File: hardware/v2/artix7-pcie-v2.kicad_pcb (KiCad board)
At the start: 4 copper layers, 60 x 51 mm, 183 parts, among them J1 Conn_02x20_Odd_Even, J10 USB_B_Micro, J2 Conn_02x20_Odd_Even, J3 JTAG_EN, J4 USB3_A, J5 USB3_A_AS_PCIE, J6 JTAG, J7 Conn_01x02, J8 SER, SW1 PROG, SW2 SW_SPST, U1 XC7A75T-FGG484, U2 W25Q64JVSSIM, U3 LP5907MFX, U4 5P49V6965A000NLGI, U5 TPS82130SILT, U6 TPS82150SILT, U7 TPS82150SILT, U8 TPS82130SILT, U9 TPS82150SILT, X1 25MHz/10pF

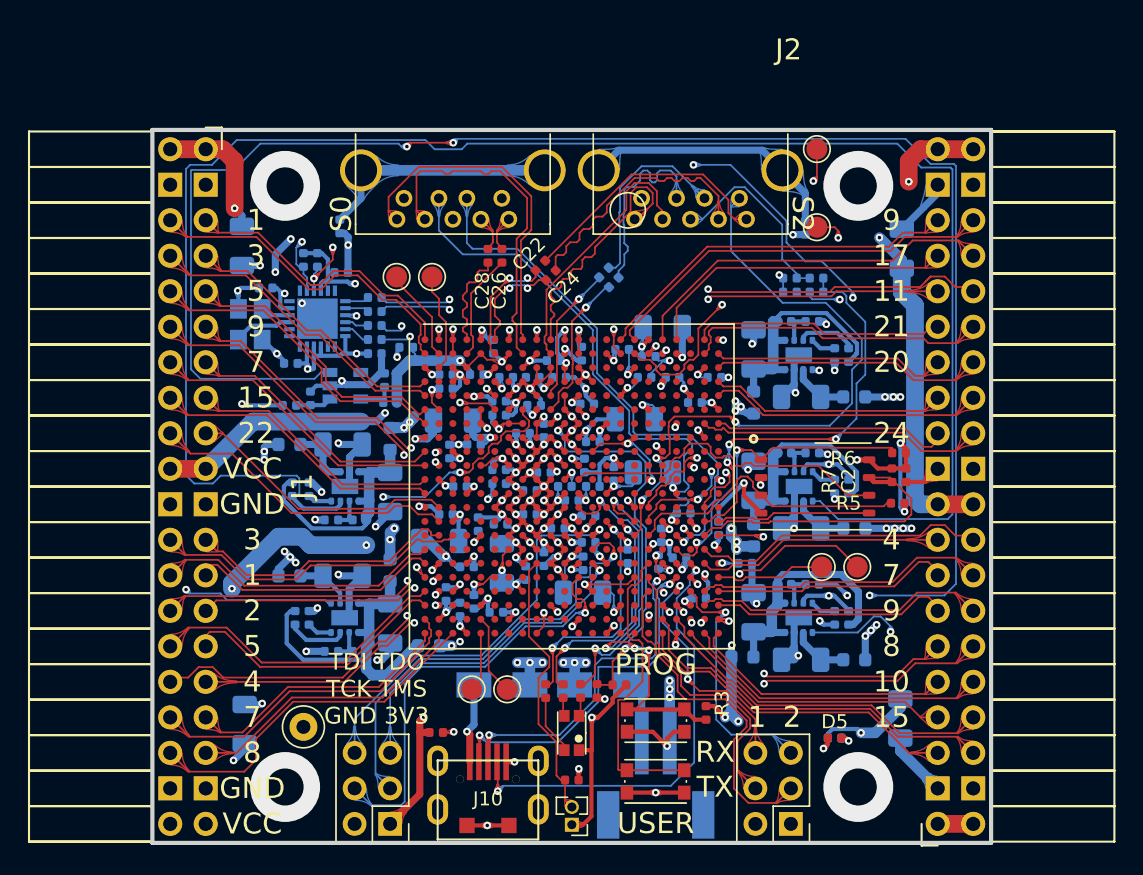
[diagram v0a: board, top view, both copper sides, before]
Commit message: v2 progress commit : serdes lanes all deskewed
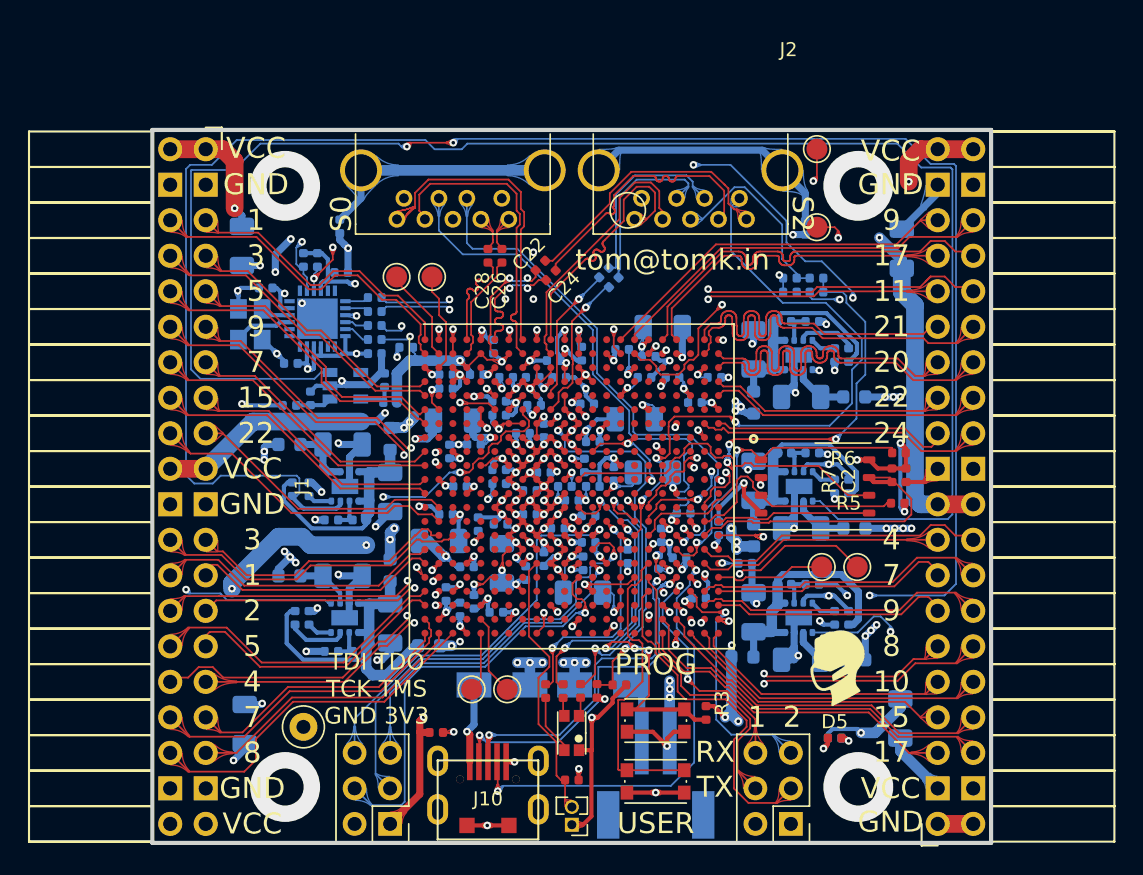
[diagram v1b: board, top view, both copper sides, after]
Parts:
- added G***: LOGO, artix7-pcie-v2:mask, F.Cu at (160.1, 99.8)
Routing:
- net /artix7-pcie-v2-bank14/IO_L20_16_P: track 19.4 -> 29.0 mm
- net /artix7-pcie-v2-bank14/IO_L20_16_N: track 16.7 -> 26.3 mm
- net /artix7-pcie-v2-bank14/IO_L21_16_P: track 21.8 -> 28.9 mm
- net /artix7-pcie-v2-bank14/IO_L21_16_N: track 18.1 -> 25.2 mm
- net /artix7-pcie-v2-serdes/S0_RX_N: track 24.5 -> 21.8 mm
- net /artix7-pcie-v2-serdes/S0_RX_P: track 24.4 -> 21.8 mm
- net /artix7-pcie-v2-bank14/IO_L17_16_N: track 22.5 -> 25.1 mm
- net /artix7-pcie-v2-bank14/IO_L17_16_P: track 26.6 -> 28.9 mm
- net /artix7-pcie-v2-serdes/MGTREFCLK1_C_P: track 14.3 -> 12.8 mm
- net /artix7-pcie-v2-serdes/MGTREFCLK1_C_N: track 14.9 -> 13.5 mm
- net /artix7-pcie-v2-serdes/S2_TX_C_N: track 7.61 -> 8.93 mm
- net /artix7-pcie-v2-serdes/S2_TX_N: track 18.8 -> 19.5 mm
- net /artix7-pcie-v2-bank14/IO_L9_16_P: track 28.7 -> 28.1 mm
- net /artix7-pcie-v2-serdes/S2_TX_P: track 18.8 -> 19.5 mm
- net GND: track 260.2 -> 260.3 mm, vias 122 -> 125
- added copper zone on Pwr.Cu, net GND
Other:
- net class J1_J2_DP0.5/0.5 added: clearance 0.127, trace_width 0.127, via_dia 0.55, via_drill 0.25
- board text added: "tom@tomk.in"

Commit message: v2 hardware: J2 differential pairs tuned
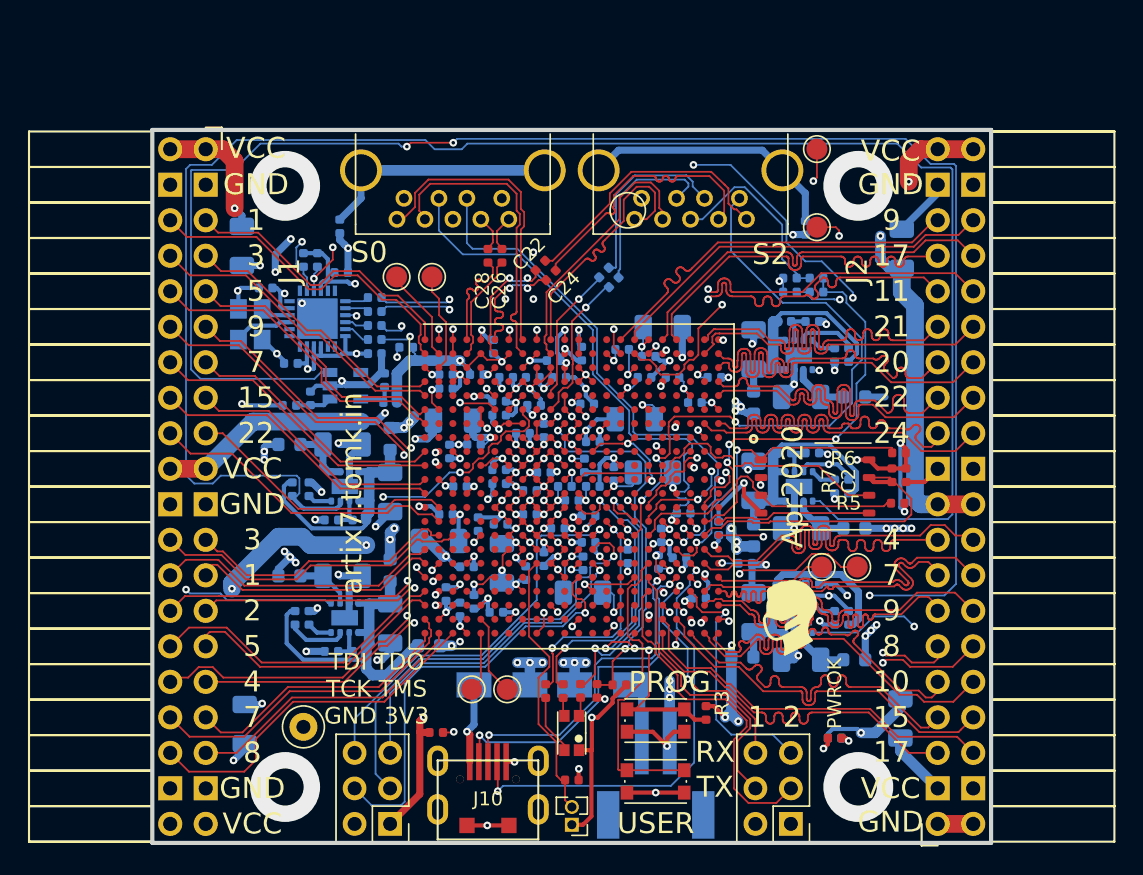
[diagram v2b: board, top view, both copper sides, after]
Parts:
- moved G*** 4.95 mm to (156.7, 96.2)
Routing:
- net /artix7-pcie-v2-bank14/IO_L22_16_N: track 16.9 -> 27.9 mm
- net /artix7-pcie-v2-bank14/IO_L24_16_N: track 17.1 -> 27.8 mm
- net /artix7-pcie-v2-bank14/IO_L9_14_N: track 17.1 -> 27.3 mm
- net /artix7-pcie-v2-bank14/IO_L7_14_N: track 17.1 -> 27.3 mm
- net /artix7-pcie-v2-bank14/IO_L4_14_N: track 17.7 -> 27.3 mm
- net /artix7-pcie-v2-bank14/IO_L10_14_N: track 18.9 -> 27.3 mm
- net /artix7-pcie-v2-bank14/IO_L22_16_P: track 19.6 -> 28.0 mm
- net /artix7-pcie-v2-bank14/IO_L24_16_P: track 20.7 -> 27.9 mm
- net /artix7-pcie-v2-bank14/IO_L15_14_N: track 20.2 -> 26.9 mm
- net /artix7-pcie-v2-bank14/IO_L8_14_N: track 20.5 -> 27.2 mm
- net /artix7-pcie-v2-bank14/IO_L9_14_P: track 20.8 -> 27.2 mm
- net /artix7-pcie-v2-bank14/IO_L7_14_P: track 20.9 -> 27.3 mm
- net /artix7-pcie-v2-bank14/IO_L4_14_P: track 21.2 -> 27.4 mm
- net /artix7-pcie-v2-bank14/IO_L11_16_N: track 22.7 -> 28.0 mm
- net /artix7-pcie-v2-bank14/IO_L10_14_P: track 22.0 -> 27.3 mm
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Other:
- net class J1_J2_DP0.5/0.5 removed
- net class J2_14_DP0.5/0.5 added: clearance 0.127, trace_width 0.127, via_dia 0.55, via_drill 0.25
- net class J2_16_DP0.5/0.5 added: clearance 0.127, trace_width 0.127, via_dia 0.55, via_drill 0.25
- board text added: "Apr2020"
- board text added: "PWROK"
- board text added: "artix7.tomk.in"
- board text removed: "tom@tomk.in"

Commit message: v2 hardware: j2_34 diff pairs matched, fix 0402 resistor packages, dropped paste from DNP resistors
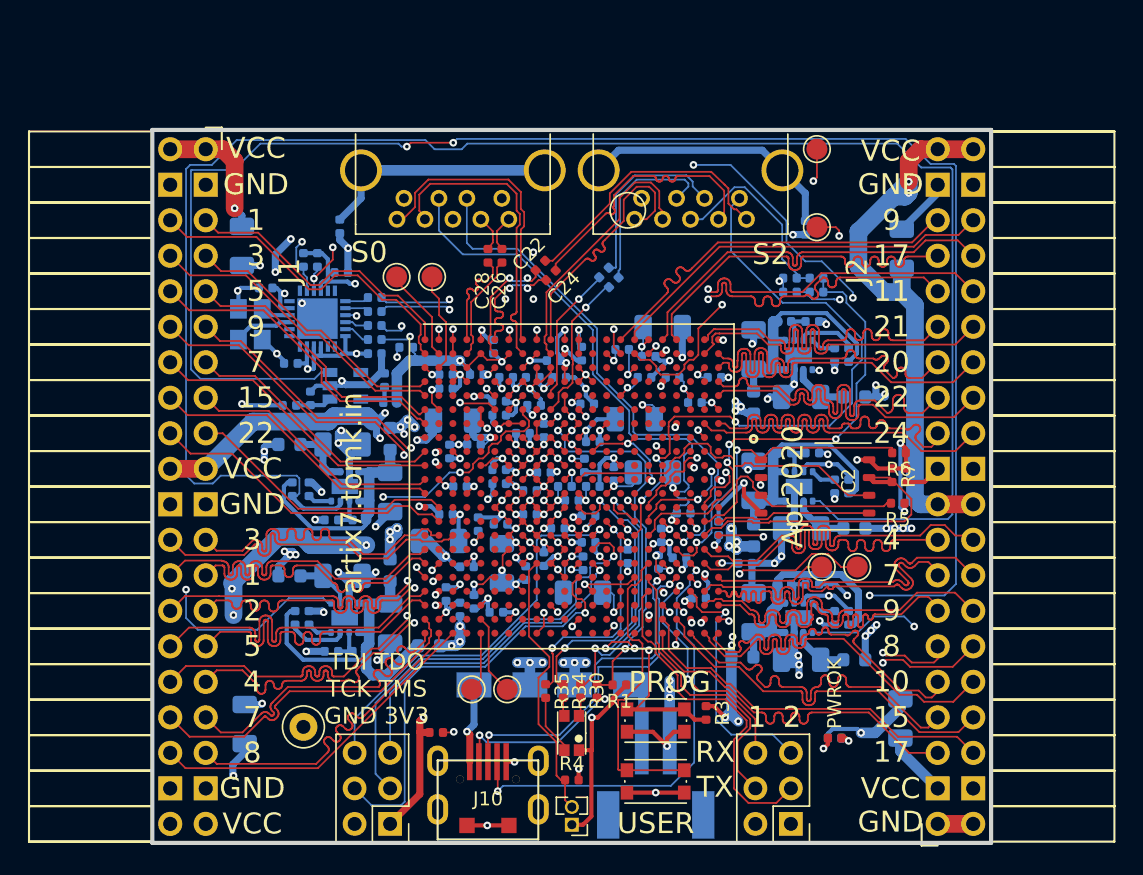
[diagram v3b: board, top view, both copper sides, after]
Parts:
- removed G***: LOGO, artix7-pcie-v2:mask
- R1, R10, R12, R13, R14, R16, R17, R18, R2, R22, R23, R24, R25, R26, R27, R28, R29, R3, R30, R31, R32, R34, R35, R36, R37, R38, R39, R4, R43, R45, R5, R51, R6, R7, R8, R9: footprint tom-passives:C_0402_1005Metric -> tom-passives:R_0402_1005Metric
- R11, R15, R33, R40, R41, R46, R47, R48, R49: footprint tom-passives:C_0603_1608Metric -> tom-passives:R_0603_1608Metric_NoPaste
- R19, R21: footprint tom-passives:R_0603_1608Metric -> tom-passives:R_0603_1608Metric_NoPaste
- R20, R42, R44, R50: footprint tom-passives:C_0402_1005Metric -> tom-passives:R_0402_1005Metric_NoPaste
- SW2: value SW_SPST -> USER
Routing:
- net GND: track 259.8 -> 274.3 mm, vias 125 -> 127
- net /VCCO_16: track 81.2 -> 92.6 mm
- net /artix7-pcie-v2-bank34/IO_L1_34_N: track 18.1 -> 24.7 mm
- net /artix7-pcie-v2-bank34/IO_L2_34_N: track 18.1 -> 24.6 mm
- net /artix7-pcie-v2-bank34/IO_L4_34_N: track 19.3 -> 24.7 mm
- net /artix7-pcie-v2-bank34/IO_L7_34_N: track 19.4 -> 24.7 mm
- net /artix7-pcie-v2-bank34/IO_L3_34_N: track 19.4 -> 24.7 mm
- net /artix7-pcie-v2-bank34/IO_L5_34_N: track 19.7 -> 24.7 mm
- net /artix7-pcie-v2-bank34/IO_L1_34_P: track 20.5 -> 24.7 mm
- net /artix7-pcie-v2-bank34/IO_L8_34_N: track 20.6 -> 24.7 mm
- net /artix7-pcie-v2-bank34/IO_L2_34_P: track 20.8 -> 24.7 mm
- net /VCCO_35: track 93.5 -> 97.1 mm, vias 10 -> 12
- net /Power/PG_1.8V: track 161.9 -> 165.3 mm
- net /artix7-pcie-v2-bank34/IO_L5_34_P: track 21.9 -> 24.7 mm
- net VCC: track 102.4 -> 104.6 mm, vias 18 -> 20
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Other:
- net class J1_34_DP0.5/0.5 added: clearance 0.127, trace_width 0.127, via_dia 0.55, via_drill 0.25
- net class J1_35_DP0.5/0.5 added: clearance 0.127, trace_width 0.127, via_dia 0.55, via_drill 0.25

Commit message: v2 hardware : add missing mounting holes, all pairs tuned and passing. J1_34_DP0.5/0.5 -> MEETS INTER-PAIR TOLERANCE 0.5000 mm (current delta 0.4093)     /artix7-pcie-v2-bank34/IO_L1_34 meets intra-pair tolerance 0.5000 mm (current delta 0.0001)     /artix7-pcie-v2-bank34/IO_L2_34 meets intra-pair tolerance 0.5000 mm (current delta 0.0740)     /artix7-pcie-v2-bank34/IO_L3_34 meets intra-pair tolerance 0.5000 mm (current delta 0.0001)     /artix7-pcie-v2-bank34/IO_L4_34 meets intra-pair tolerance 0.5000 mm (current delta 0.0799)     /artix7-pcie-v2-bank34/IO_L5_34 meets intra-pair tolerance 0.5000 mm (current delta 0.0000)     /artix7-pcie-v2-bank34/IO_L7_34 meets intra-pair tolerance 0.5000 mm (current delta 0.0000)     /artix7-pcie-v2-bank34/IO_L8_34 meets intra-pair tolerance 0.5000 mm (current delta 0.0465) J1_35_DP0.5/0.5 -> MEETS INTER-PAIR TOLERANCE 0.5000 mm (current delta 0.1851)     /artix7-pcie-v2-bank34/IO_L15_35 meets intra-pair tolerance 0.5000 mm (current delta 0.0000)     /artix7-pcie-v2-bank34/IO_L1_35 meets intra-pair tolerance 0.5000 mm (current delta 0.0000)     /artix7-pcie-v2-bank34/IO_L22_35 meets intra-pair tolerance 0.5000 mm (current delta 0.0000)     /artix7-pcie-v2-bank34/IO_L3_35 meets intra-pair tolerance 0.5000 mm (current delta 0.0000)     /artix7-pcie-v2-bank34/IO_L5_35 meets intra-pair tolerance 0.5000 mm (current delta 0.0000)     /artix7-pcie-v2-bank34/IO_L7_35 meets intra-pair tolerance 0.5000 mm (current delta 0.0000)     /artix7-pcie-v2-bank34/IO_L9_35 meets intra-pair tolerance 0.5000 mm (current delta 0.0000) J2_14_DP0.5/0.5 -> MEETS INTER-PAIR TOLERANCE 0.5000 mm (current delta 0.4675)     /artix7-pcie-v2-bank14/IO_L10_14 meets intra-pair tolerance 0.5000 mm (current delta 0.0304)     /artix7-pcie-v2-bank14/IO_L15_14 meets intra-pair tolerance 0.5000 mm (current delta 0.0001)     /artix7-pcie-v2-bank14/IO_L17_14 meets intra-pair tolerance 0.5000 mm (current delta 0.0001)     /artix7-pcie-v2-bank14/IO_L4_14 meets intra-pair to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
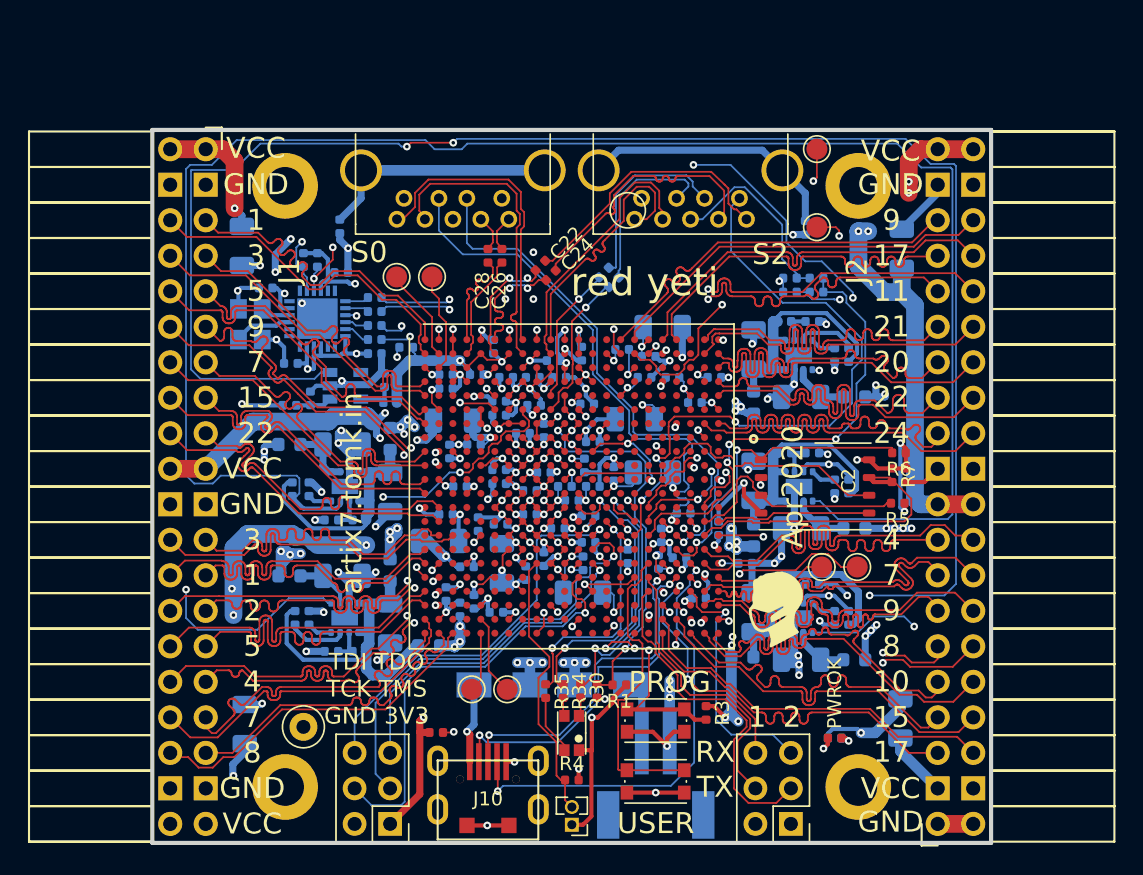
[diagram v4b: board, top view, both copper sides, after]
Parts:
- added H1: mask silk image, artix7-pcie-v2:mask, F.Cu at (155.7, 95.6)
- added TP10: TestPoint, tom-mechanical:MountingHole_2.7mm_M2.5_DIN965_Pad, F.Cu at (120.6, 65.3)
- added TP11: TestPoint, tom-mechanical:MountingHole_2.7mm_M2.5_DIN965_Pad, F.Cu at (120.6, 108.3)
- added TP12: TestPoint, tom-mechanical:MountingHole_2.7mm_M2.5_DIN965_Pad, F.Cu at (161.6, 65.3)
- added TP13: TestPoint, tom-mechanical:MountingHole_2.7mm_M2.5_DIN965_Pad, F.Cu at (161.6, 108.3)
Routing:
- net /artix7-pcie-v2-bank34/IO_L15_35_N: track 18.4 -> 24.1 mm
- net /artix7-pcie-v2-bank34/IO_L7_35_N: track 18.9 -> 24.1 mm
- net /artix7-pcie-v2-bank34/IO_L22_35_N: track 19.4 -> 24.1 mm
- net /artix7-pcie-v2-bank34/IO_L3_35_N: track 19.7 -> 24.1 mm
- net /artix7-pcie-v2-bank34/IO_L5_35_N: track 20.1 -> 24.1 mm
- net /artix7-pcie-v2-bank34/IO_L9_35_N: track 20.8 -> 24.3 mm
- net /artix7-pcie-v2-bank34/IO_L1_35_N: track 20.8 -> 24.2 mm
- net /artix7-pcie-v2-bank34/IO_L15_35_P: track 21.1 -> 24.1 mm
- net /artix7-pcie-v2-bank34/IO_L7_35_P: track 21.3 -> 24.1 mm
- net /VCCO_16: track 92.6 -> 90.5 mm, vias 11 -> 13
- net /artix7-pcie-v2-bank34/IO_L22_35_P: track 22.3 -> 24.1 mm
- net /artix7-pcie-v2-bank34/IO_L3_35_P: track 22.4 -> 24.1 mm
- net /VCCO_34: track 75.4 -> 76.9 mm
- net VCC: track 104.6 -> 106.0 mm
- net /artix7-pcie-v2-bank34/IO_L5_35_P: track 22.7 -> 24.1 mm
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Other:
- board text added: "red yeti"

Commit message: Apr2020 rc1
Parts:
- added R52: 100R/1%, tom-passives:R_0402_1005Metric, B.Cu at (148.4, 96.6)
- added TP14: SCL, tom-mechanical:TestPoint_Pad_D1.5mm, B.Cu at (123.6, 63.3)
- added TP15: SDA, tom-mechanical:TestPoint_Pad_D1.5mm, B.Cu at (122.6, 68.3)
- moved H1 1.29 mm to (156.7, 96.4)
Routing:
- net /CLK_SCL: track 49.1 -> 55.6 mm
- net /artix7-pcie-v2-bank14/IO_L12_14_P: track 17.4 -> 20.1 mm, vias 2 -> 1
- net /CLK_SDA: track 53.6 -> 54.9 mm
- net /CLKIN_N: track 50.5 -> 51.4 mm
- net /CLKIN_P: track 50.5 -> 51.4 mm
- net /artix7-pcie-v2-bank14/IO_L11_14_P: track 32.6 -> 33.4 mm
